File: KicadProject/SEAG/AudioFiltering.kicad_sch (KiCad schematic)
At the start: 10 parts, among them J11 Screw_Terminal_01x02, J12 Screw_Terminal_01x02

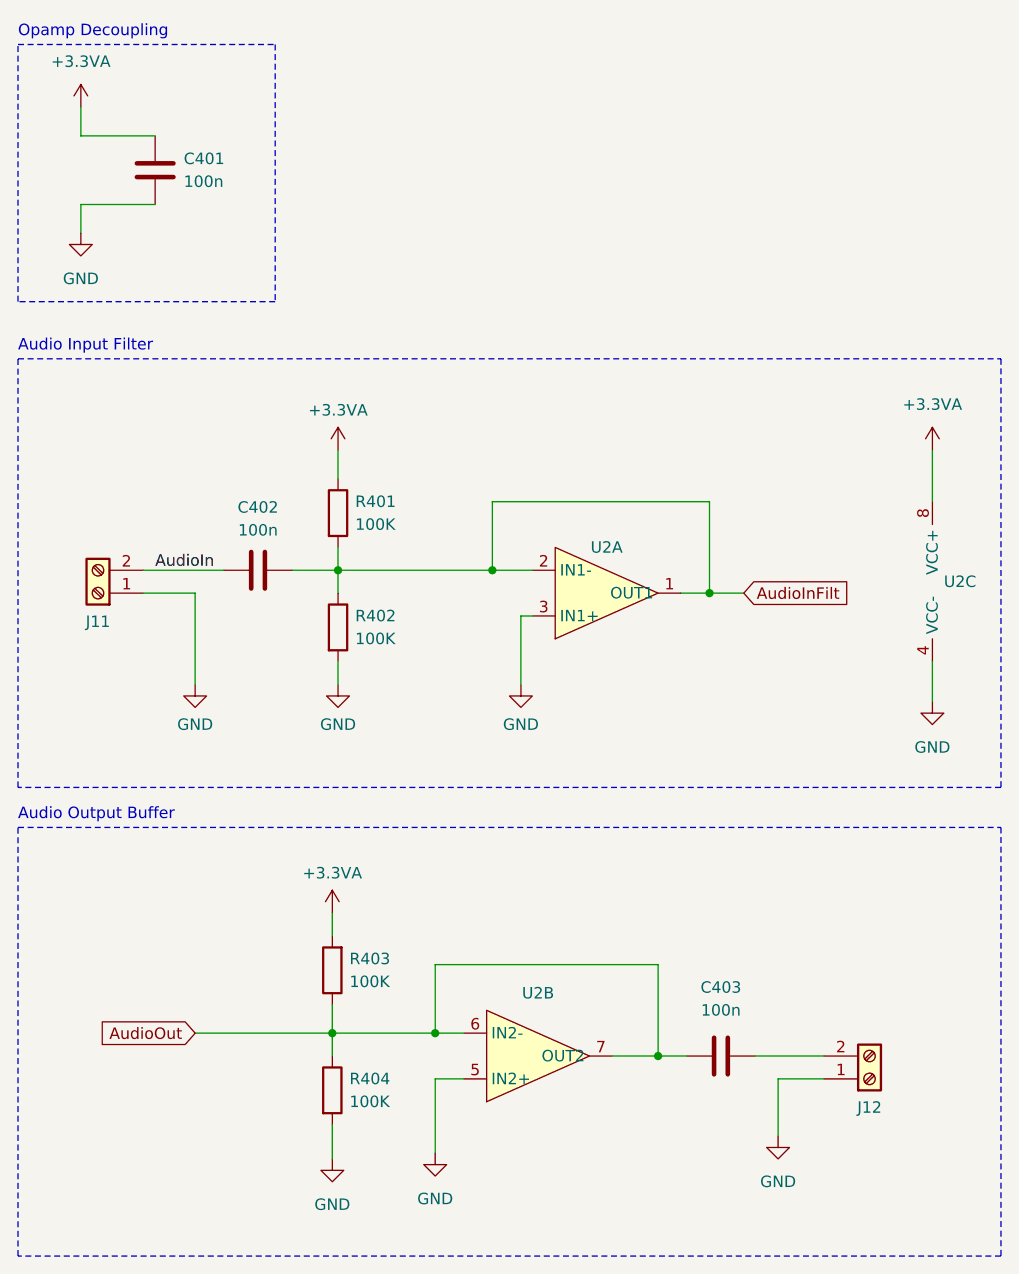
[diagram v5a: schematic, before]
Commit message: Added flanger, chorus (both kinda scuffed), added methods to change filter level. added Filter struct to represent a filter with its methods
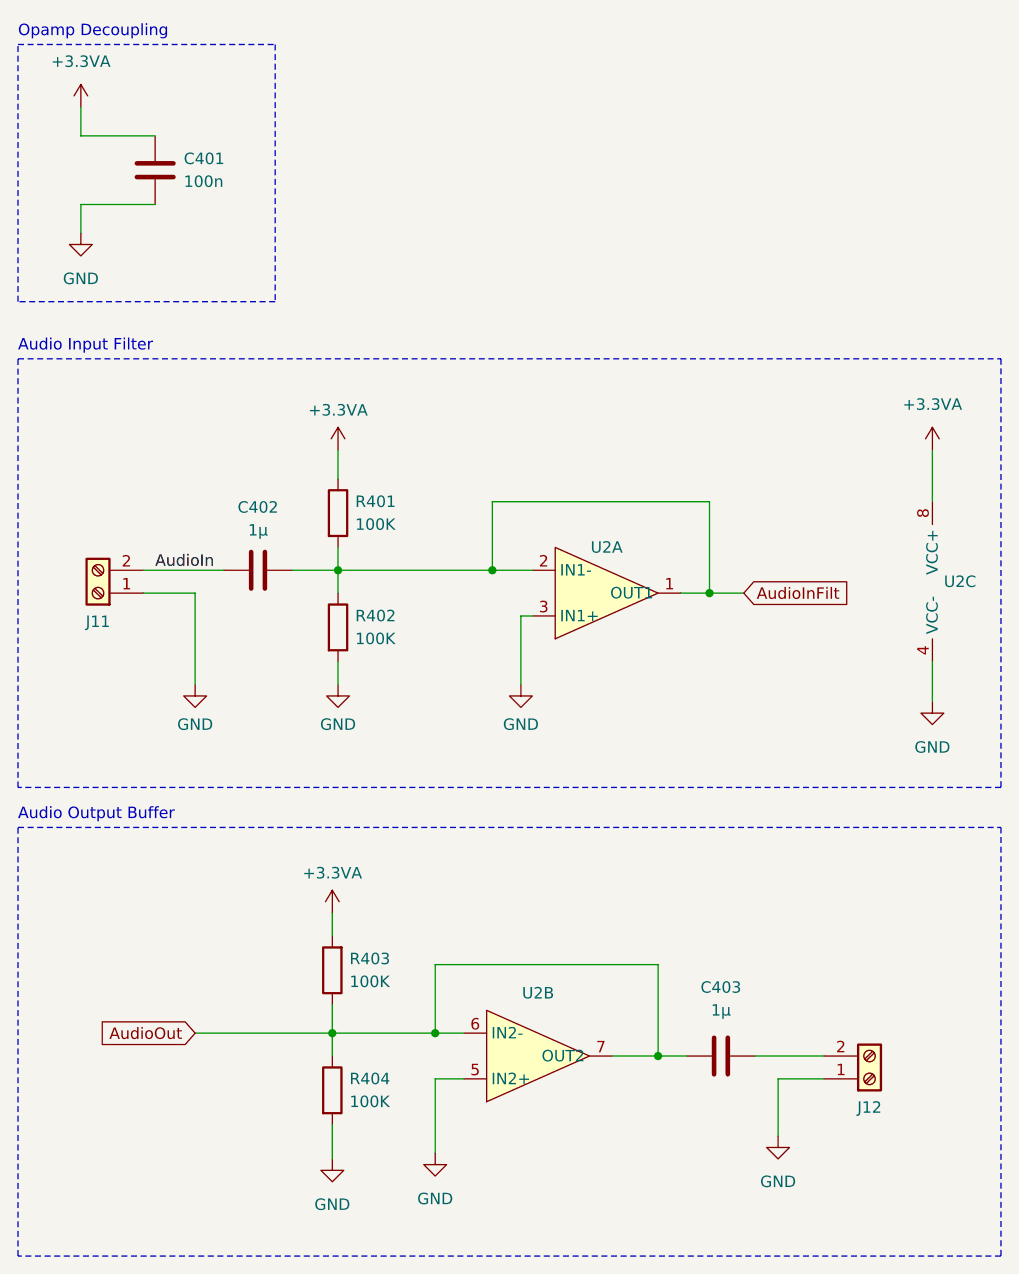
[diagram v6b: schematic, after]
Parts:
- C402, C403: value 100n -> 1µ
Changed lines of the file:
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@@
       (effects (font (size 1.27 1.27)))
     )
-    (property "Value" "100n" (at 43.815 74.93 90)
+    (property "Value" "1µ" (at 43.815 74.93 90)
       (effects (font (size 1.27 1.27)))
     )
@@
       (effects (font (size 1.27 1.27)))
     )
-    (property "Value" "100n" (at 95.25 128.27 90)
-      (effects (font (size 1.27 1.27)))
-    )
+    (property "Value" "1µ" (at 95.25 128.27 90)
+      (effects (font (size 1.27 1.27)))
+    )
